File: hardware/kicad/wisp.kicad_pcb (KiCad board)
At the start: 2 copper layers, 100 x 100 mm, 73 parts, among them J1 USB-C, J2 Second I2C Bus, J3 mmWave UART (LD2410), J4 I2S Mic (INMP441), J5 Switched DC Output, J6 Reed/Hall Contact, J7 1-Wire Bus, J8 Analog Sensor Pad, J9 Expansion Header, Q1 MMBT3904, Q2 MMBT3904, Q3 2N7002, Q4 MMBT3904, SW1 RESET, SW2 BOOT, U1 CH340C, U2 AP63203WU-7, U3 ESP32-WROOM-32, U4 SCD41-D-R2, U5 BME680, U6 BH1750FVI-TR

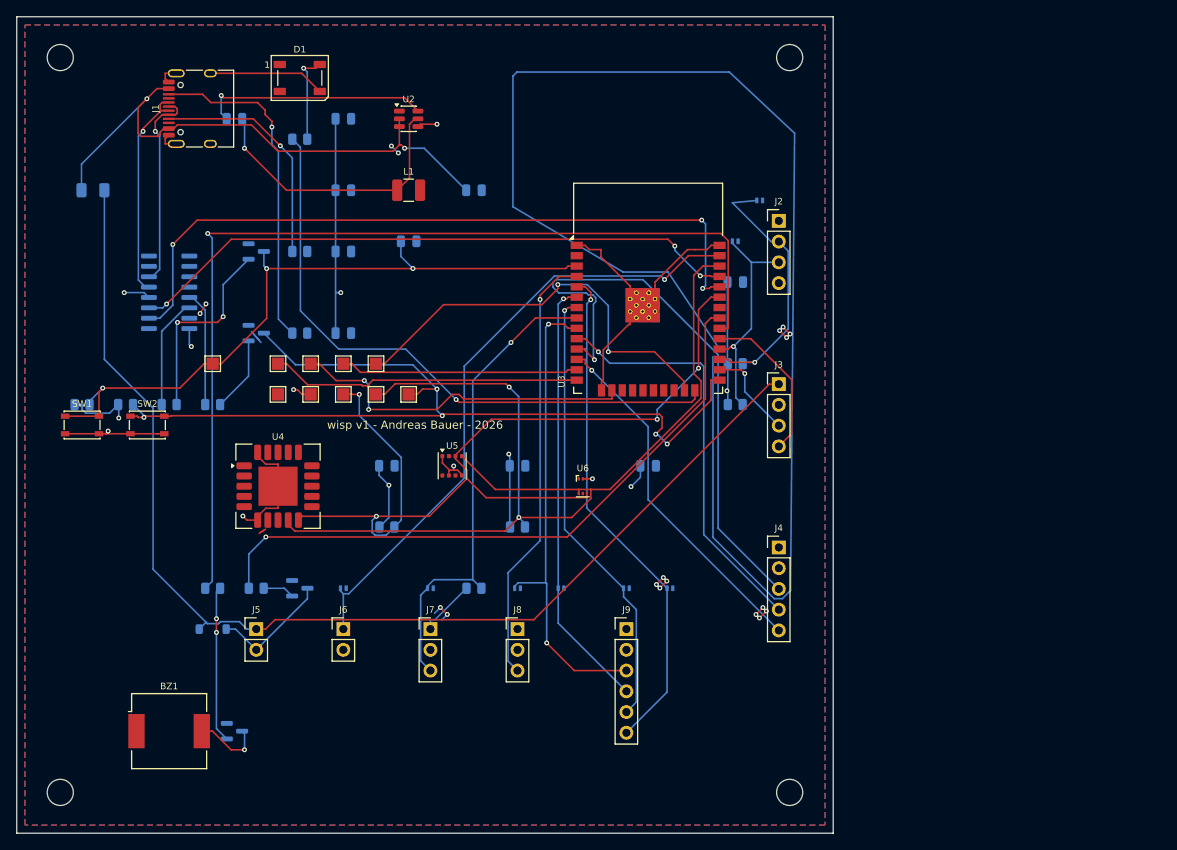
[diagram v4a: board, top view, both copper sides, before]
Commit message: Close 1 more GND/+3V3 gap by rerouting /+5V_EXT around the U5/U6 cluster
Prompted by a placement-quality review: checked whether the layout
follows best practice rather than assuming prior scaling passes got it
right. Found a real issue (decoupling caps C8-C11 sit 8-13mm from their
IC's +3V3 pin, well past the ~2-3mm recommended for effective local
filtering) and a real fix for the remaining pour-stitch gaps.

Tried moving the decoupling caps to <3mm of their ICs and re-routing:
verified clean on its own, but the resulting route converged on 11
unconnected pour islands, worse than the 5 already achieved. A floating
power pin is a more severe defect than a suboptimal-but-present
decoupling cap, so this was reverted -- documented in hardware/README.md
as a real, known issue for a future layout pass rather than dropped
silently.

Also tried a non-uniform 90x90mm regrow (shrink the board while pushing
extra room specifically around U5/U6): worse result (8 unconnected), and
U6 still had zero +3V3 connections either way, confirming U6's problem
is intrinsic to its own pad geometry, not board-level placement density.
Reverted.

What worked: /+5V_EXT (connecting F1, D4, and two DNP headers at
opposite board corners) was the direct blocker behind most remaining
gaps -- Freerouting had no reason to route it around the U5/U6 sensor
cluster since it doesn't know that area needs to stay clear for later
pour access. Ripped up just this net and re-routed it with A* pathfinding
under an explicit local keepout around U5+U6, forcing it around the
cluster. Re-running the stitching passes afterward closed D9's GND pad.

Result: 5 of 26 original gaps remain (U5 pads 2/6, U6 pads 1/5). U5 keeps
a third connected +3V3 pin so it stays functional; U6 has only two +3V3
pins and both are open, so U6 currently has no power connection at all --
not fab-ready until that's resolved. Next lever: increase U6's pad copper
area (no fab-tier cost, needs checking against its datasheet land
pattern firs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
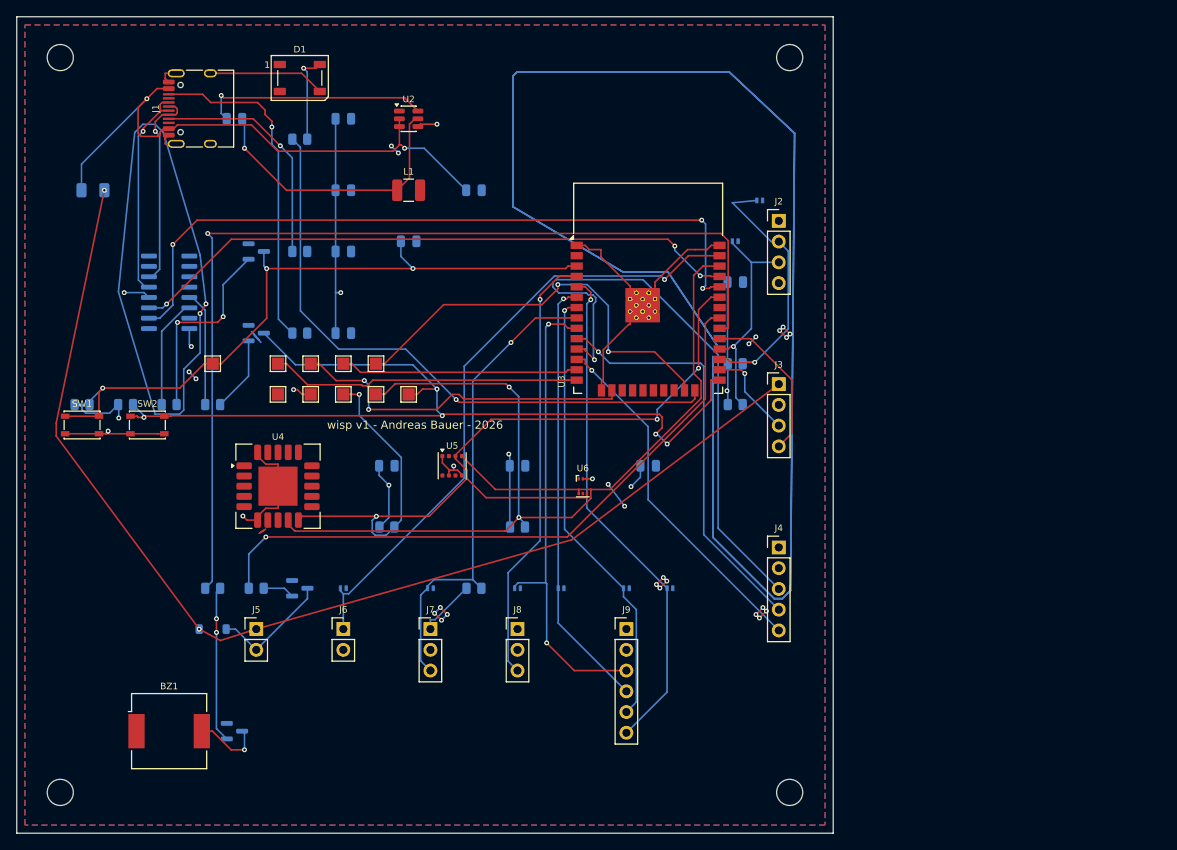
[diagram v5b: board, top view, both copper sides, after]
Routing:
- net GND: track 291.6 -> 548.9 mm, vias 22 -> 24
- net +3V3: track 86.2 -> 91.9 mm, vias 10 -> 16
- net /+5V_EXT: track 142.4 -> 139.6 mm, vias 0 -> 2
